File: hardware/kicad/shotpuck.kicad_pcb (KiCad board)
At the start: 2 copper layers, 37 x 37 mm, 27 parts, among them J1 Magnetic pogo 2P (female), J2 TC2030-NL, Q1 DMN63D8LDW, U1 MDBT50Q-512K, U2 LIS2DE12TR, U3 MCP73831T-2ACI/OT

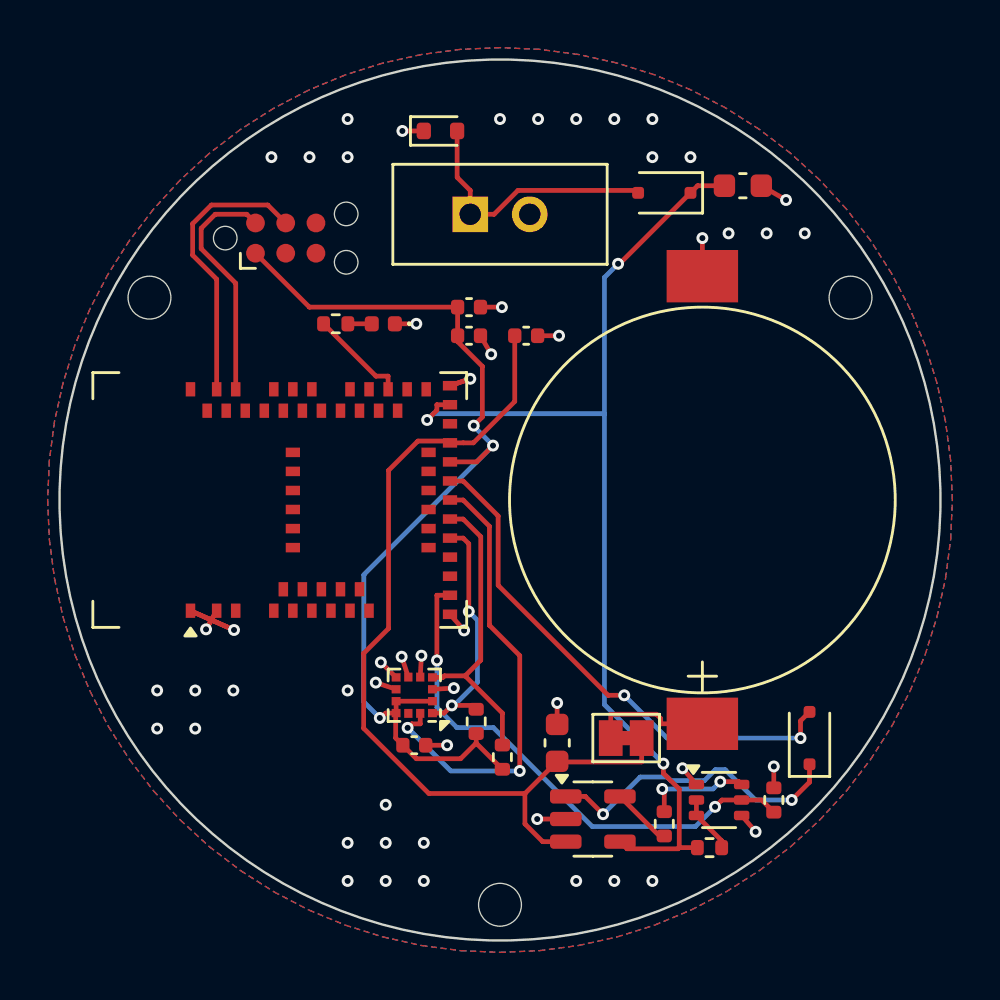
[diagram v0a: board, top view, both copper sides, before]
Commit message: Update ShotPuck to v0.2 design package
Enhancements include the integration of the LSM6DSO32 IMU, which replaces the LIS2DE12 accelerometer, allowing for 6-axis motion capture. The new CAPTURE characteristic streams raw data around each shot, improving performance metrics. The firmware and simulation have been updated to support these changes, including adjustments to the BLE protocol (v2) for better data handling. Additionally, the toolchain has been migrated to a native Windows environment for development.

Key changes:
- Updated deliverable status to v0.2.
- Added capture functionality for bow motion.
- Adjusted simulation and validation processes to reflect new hardware capabilities.
- Enhanced documentation to include new features and user requirements.

Co-Authored-By: Claude Opus 5.5 <noreply@anthropic.com>
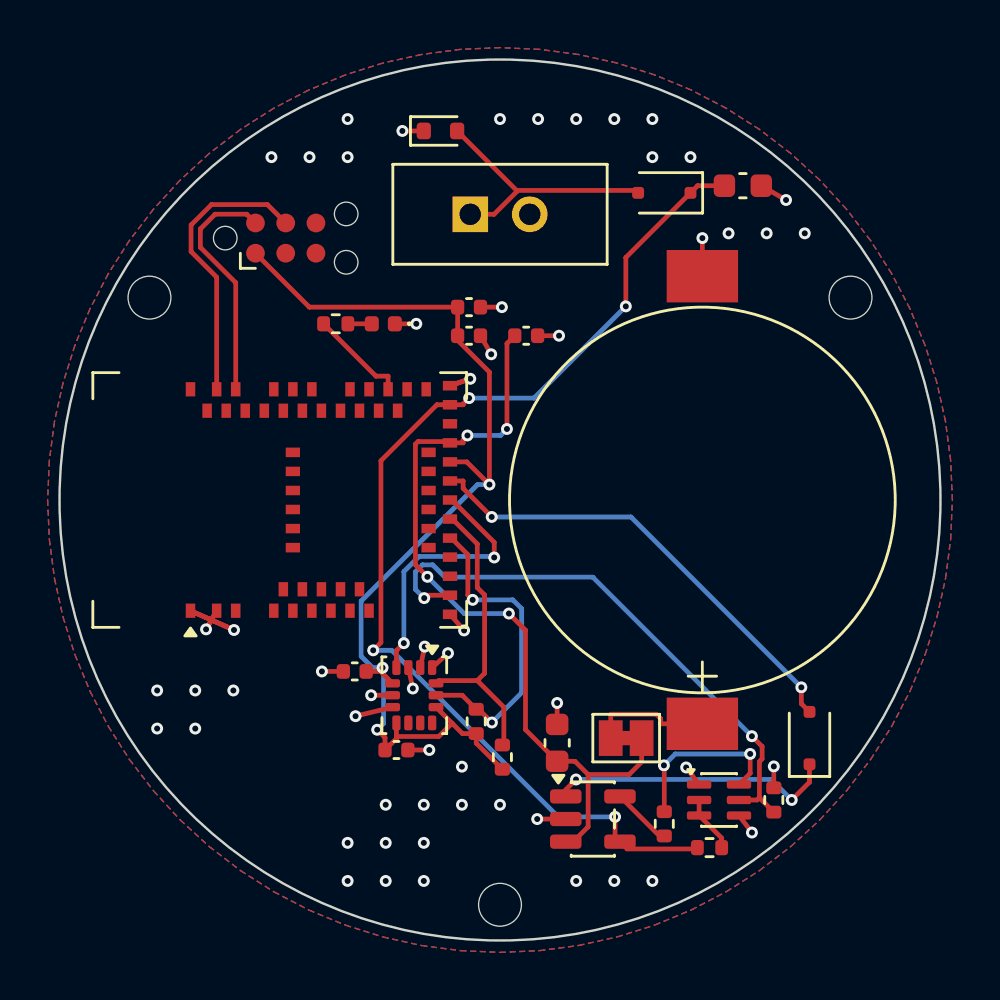
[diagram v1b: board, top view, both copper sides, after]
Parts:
- added C7: 100n, Capacitor_SMD:C_0402_1005Metric, F.Cu at (-4.35, 10.5)
- U2: value LIS2DE12TR -> LSM6DSO32TR; footprint Package_LGA:LGA-12_2x2mm_P0.5mm -> Package_LGA:LGA-14_3x2.5mm_P0.5mm_LayoutBorder3x4y
- moved C6 3.98 mm to (-6.10, 7.20), turned to 180 degrees
- turned U2 to -90 degrees
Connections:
- U2 pad 1: SCL -> GND
- U2 pad 10: VDD -> (no net)
- U2 pad 12: ACC_INT1 -> VDD
- U2 pad 2: VDD -> GND
- U2 pad 4: SDA -> ACC_INT1
- U2 pad 5: GND -> VDD
- U2 pad 8: GND -> VDD
- U2 pad 9: VDD -> (no net)
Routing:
- net ACC_INT1: track 19.4 -> 11.5 mm
- net VBAT: track 38.3 -> 33.6 mm, vias 0 -> 4
- net SCL: track 10.4 -> 13.4 mm
- net PROG_SW: track 4.50 -> 7.25 mm
- net CHG_STAT: track 22.2 -> 19.7 mm
- net CHG_INH: track 22.2 -> 24.2 mm
- net VIN: track 44.2 -> 46.1 mm, vias 3 -> 4
- net GND: track 26.0 -> 27.6 mm, vias 52 -> 56
- net VDD: track 42.0 -> 43.6 mm
- net STAT: track 13.0 -> 12.1 mm

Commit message: Add OTA, nRF52840, PCM, magnetic connector, Ø36 board and JLC panel
- Firmware: nRF52840 module (MDBT50Q-1MV2), MCUboot swap-using-move with
  ECDSA-P256 signed images, MCUmgr SMP over encrypted BLE, watchdog and
  self-confirm; 1 MB flash layout; release images shotpuck_full.hex and
  shotpuck_update.bin (v0.2.0).
- Hardware: BQ29700 + DMN2004DWK cell protection, universal CP1654 pads,
  Samzo magnetic 2-pin connector, Ø36 mm board inside the Ø40 mm puck,
  0.3 mm vias, 2x2 KiKit panel and JLCPCB BOM/CPL (gen_panel.py, gen_jlc.py).
- Mechanical: cavity sized for Varta CP1654 swell, connector chimney,
  optional brass Ø8 trim pins (balance reported with and without them).
- gen_pcb.py: stitching after all routing, connectivity rebuilt before fills,
  pre-routed Q2 drain and Q1 GND links, Freerouting optimizer off, up to 4
  board attempts until nothing is unconnected. DRC 0/0, panel DRC 0/0.

Co-Authored-By: Claude Opus 5.5 <noreply@anthropic.com>
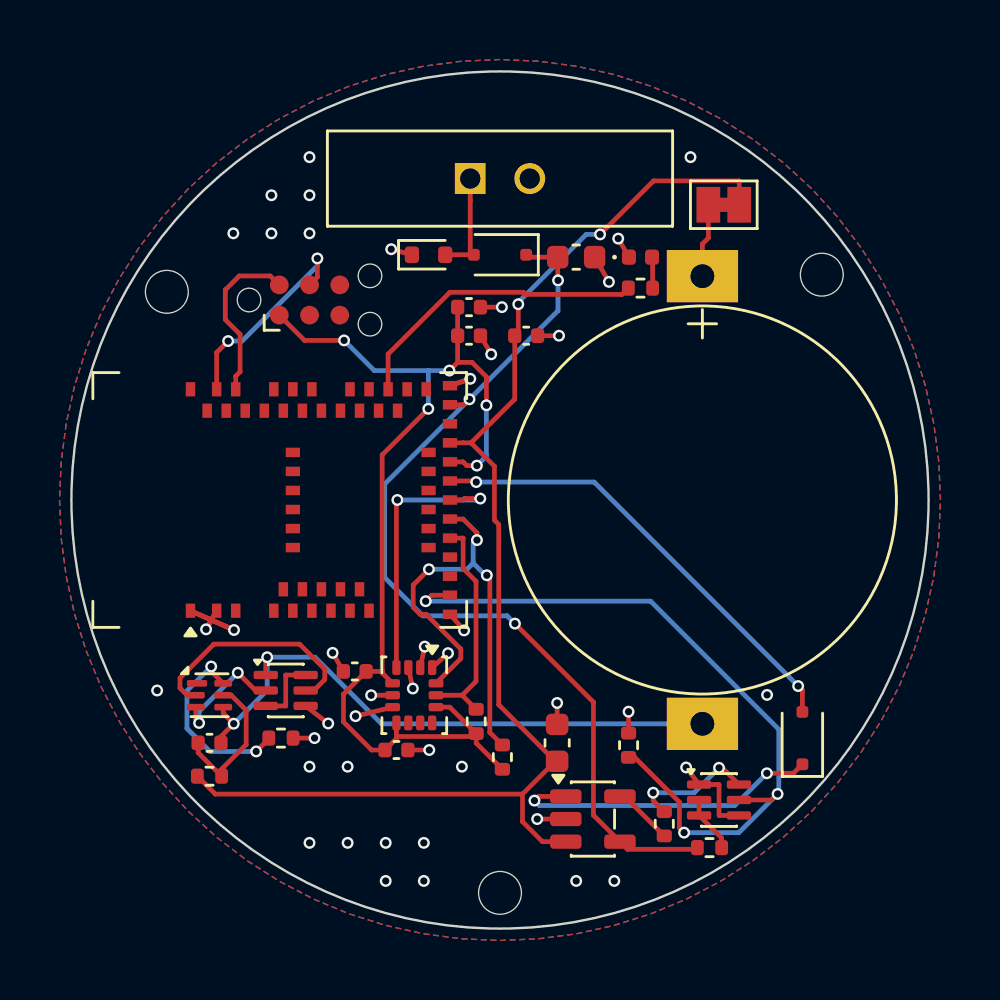
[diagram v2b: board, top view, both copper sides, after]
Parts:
- added C8: 100n, Capacitor_SMD:C_0402_1005Metric, F.Cu at (-12.2, 10.2)
- added Q2: DMN2004DWK, Package_TO_SOT_SMD:SOT-363_SC-70-6, F.Cu at (-9.00, 8.00)
- added R7: 330R, Resistor_SMD:R_0402_1005Metric, F.Cu at (-12.2, 11.6)
- added R8: 2.2k, Resistor_SMD:R_0402_1005Metric, F.Cu at (-9.20, 10.0)
- added U4: BQ29700DSER, Package_SON:WSON-6_1.5x1.5mm_P0.5mm, F.Cu at (-12.2, 8.20)
- BT1: value Varta CP1654 A3 (tabbed) -> Varta CP1654 A3 (wire or tag version); footprint ShotPuck:CP1654_Tabbed -> ShotPuck:CP1654_Pads
- J1: value Magnetic pogo 2P (female) -> Samzo PR5L4015-2P-C-F; footprint ShotPuck:MagPogo_2P -> ShotPuck:MagPogo_Samzo_2P
- U1: value MDBT50Q-512K -> MDBT50Q-1MV2
- moved JP1 22.8 mm to (9.40, -12.4)
- moved R4 12.9 mm to (5.90, -8.90)
- moved D4 11.2 mm to (5.90, -10.2), turned to 0 degrees
- moved C1 7.62 mm to (3.20, -10.2)
- moved D1 7.37 mm to (0.00, -10.3)
- moved R3 6.52 mm to (5.40, 10.3)
- moved D3 5.22 mm to (-3.00, -10.3)
- moved J2 2.79 mm to (-8.00, -8.40)
- moved H1 1.54 mm to (13.5, -9.46)
- moved J1 1.50 mm to (0.00, -13.5)
- moved H2 0.77 mm to (-14.0, -8.74)
- moved H3 0.50 mm to (0.00, 16.5)
- moved D2 0.30 mm to (12.7, 10.0)
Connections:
- BT1 pad 2: GND -> BAT_N
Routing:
- net BAT_N: track 0.00 -> 25.5 mm, vias 0 -> 2
- net VBAT: track 33.6 -> 54.2 mm, vias 4 -> 2
- net PCM_COUT: track 0.00 -> 9.75 mm
- net LED_IO: track 4.17 -> 12.8 mm
- net PCM_VM: track 0.00 -> 8.03 mm, vias 0 -> 2
- net CHG_INH: track 24.2 -> 31.5 mm, vias 2 -> 3
- net SDA: track 12.5 -> 19.3 mm, vias 0 -> 3
- net VIN: track 46.1 -> 39.4 mm, vias 4 -> 3
- net VIN_RAW: track 11.1 -> 4.40 mm
- net PCM_BAT: track 0.00 -> 6.23 mm
- net PCM_DOUT: track 0.00 -> 4.99 mm, vias 0 -> 2
- net SCL: track 13.4 -> 9.55 mm, vias 2 -> 0
- net SWDCLK: track 12.0 -> 8.84 mm, vias 0 -> 2
- net PCM_D: track 0.00 -> 2.98 mm
- net SWDIO: track 10.1 -> 7.17 mm
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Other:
- board size 37 x 37 mm -> 36 x 36 mm

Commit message: Seat the cell in a PCB notch open to the rim (puck 10.45 mm)
- The cell sits on the Kapton over the base in a notch in the PCB
  (Ø16.6 mm round end, open to the rim) instead of on top of the board,
  saving the 0.8 mm board thickness: 11.25 -> 10.45 mm, 19.8 g with the
  optional brass pins, 18.0 g without.
- Rounded relief on the + side lets the bottom (+ can) tab bend up to the
  + pad; cell pads moved to ±10.2 mm.
- Screw boss 35° -> 40° so its face stays on the board beside the notch;
  JP1 turned upright, D2 moved to the bottom centre (CHG_STAT had no route
  past the notch).
- gen_pcb.py builds the whole outline (rim arc, notch lines, arcs) and a
  copper keep-out along the notch; puck.py cuts the same shape.
- Assembly: full Kapton disc, foam/RTV between cell and cap wall.
- Board DRC 0/0, panel DRC 0/0, netlist PASS; fab, panel and JLC files
  regenerated.

Co-Authored-By: Claude Opus 5.5 <noreply@anthropic.com>
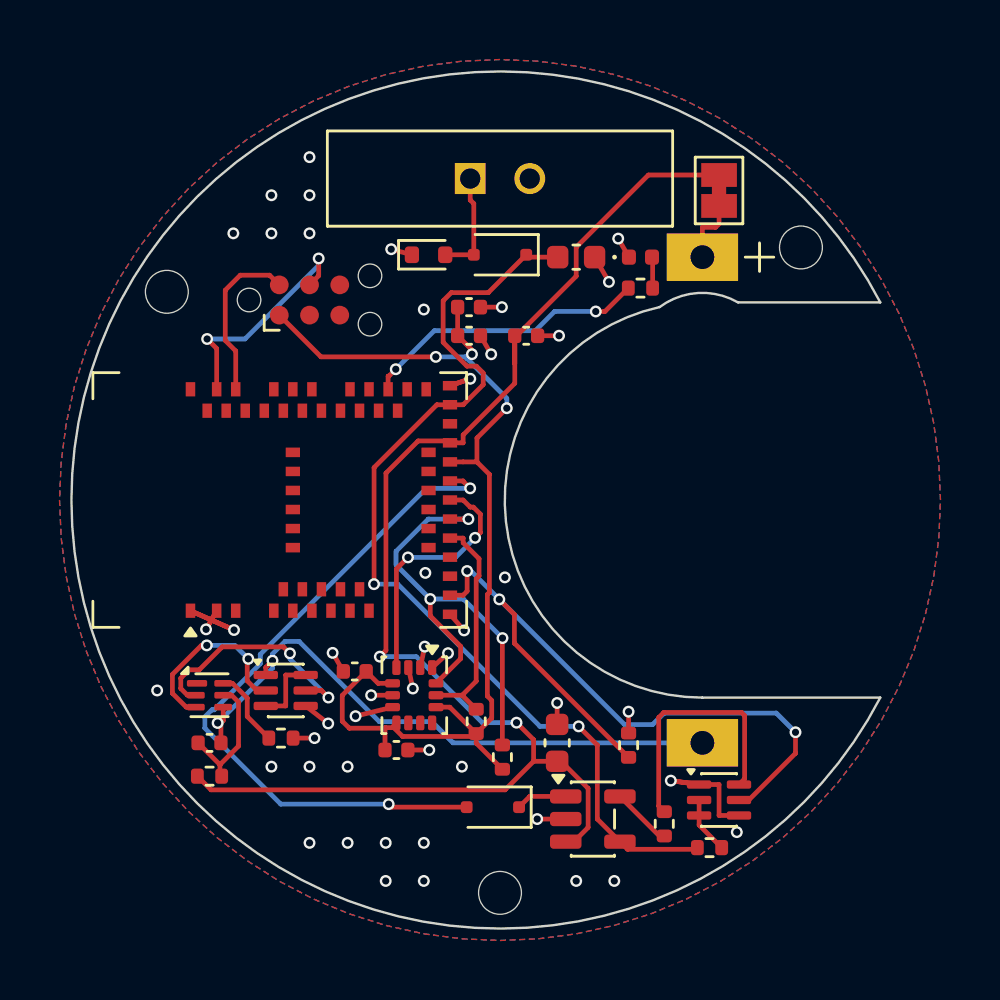
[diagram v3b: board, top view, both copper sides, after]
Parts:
- moved D2 13.3 mm to (-0.30, 12.9), turned to 180 degrees
- moved H1 1.44 mm to (12.6, -10.6)
- moved JP1 0.63 mm to (9.20, -13.0), turned to 90 degrees
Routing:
- net STAT: track 13.4 -> 2.15 mm, vias 2 -> 0
- net CHG_STAT: track 19.3 -> 29.2 mm
- net PROG_SW: track 5.32 -> 10.8 mm, vias 2 -> 0
- net VBAT: track 54.2 -> 59.5 mm
- net PCM_VM: track 8.03 -> 3.32 mm, vias 2 -> 0
- net PCM_DOUT: track 4.99 -> 7.83 mm
- net VIN: track 39.4 -> 41.1 mm, vias 3 -> 2
- net GND: track 30.2 -> 31.7 mm, vias 43 -> 46
- net ACC_INT1: track 11.9 -> 10.6 mm
- net VDD: track 45.8 -> 44.8 mm, vias 5 -> 3
- net SWDCLK: track 8.84 -> 9.80 mm
- net BAT_N: track 25.5 -> 26.3 mm
- net PCM_BAT: track 6.23 -> 5.53 mm
- net LED_IO: track 12.8 -> 12.2 mm, vias 0 -> 2
- net PCM_COUT: track 9.75 -> 10.0 mm, vias 0 -> 2
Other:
- board size 36 x 36 mm -> 34 x 36 mm

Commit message: Update ShotPuck design to rev A: replace stud with flat plate, adjust dimensions, and enhance PCB layout
- Redesigned the ShotPuck to use a 2.0 mm flat 6061 plate, bolted through a steel sleeve, improving manufacturability and cost.
- Adjusted dimensions: puck height reduced to 9.90 mm, with a center of mass 0.85 mm off-axis.
- Updated layout.json to reflect new design parameters, including cell placement and PCB notch.
- Enhanced mechanical and electrical design files, including updated battery specifications (LIR1254) and revised component placements.
- Improved documentation in HANDOVER.md and README.md to reflect changes in design and functionality.

Co-Authored-By: Claude Opus 5.5 <noreply@anthropic.com>
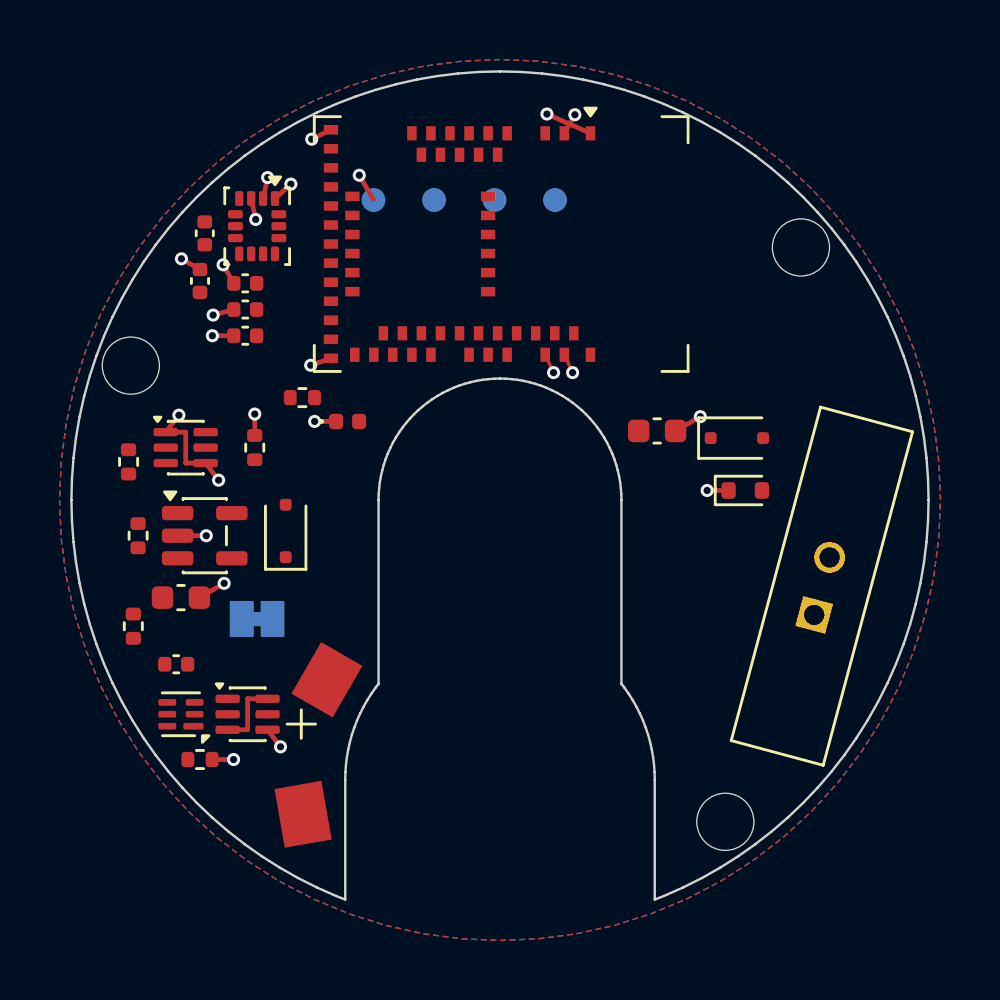
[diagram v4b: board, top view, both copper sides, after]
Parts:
- removed R5, R6: 4.7k DNP, Resistor_SMD:R_0402_1005Metric
- BT1: value Varta CP1654 A3 (wire or tag version) -> LIR1254 (plain, spring contacts); footprint ShotPuck:CP1654_Pads -> ShotPuck:LIR1254_Contacts
- H1, H2, H3: value M1.6 -> M2; footprint ShotPuck:MountingHole_1.8mm_NPTH -> ShotPuck:MountingHole_2.4mm_NPTH
- J2: value TC2030-NL -> SWD pads; footprint Connector:Tag-Connect_TC2030-IDC-NL_2x03_P1.27mm_Vertical -> ShotPuck:SWD_Pads_1x4_P2.54; moved to B.Cu
- JP1: moved to B.Cu
- R1: value 20k 1% -> 47k 1%
- moved R2 29.3 mm to (-15.6, -1.60), turned to 90 degrees
- moved Q1 26.8 mm to (-13.2, -2.20)
- moved JP1 26.5 mm to (-10.2, 5.00), turned to 180 degrees
- moved R1 25.2 mm to (-15.2, 1.50)
- moved J1 21.8 mm to (13.5, 3.62), turned to 75 degrees
- moved C7 21.4 mm to (-12.6, -9.20), turned to 90 degrees
- moved U2 20.8 mm to (-10.2, -11.5)
- moved U3 20.2 mm to (-12.4, 1.50)
- moved R3 20.1 mm to (-10.3, -2.20)
- moved C6 19.4 mm to (-12.4, -11.2), turned to 90 degrees
- moved C2 16.9 mm to (-13.4, 4.10), turned to 0 degrees
- moved D3 16.6 mm to (10.3, -0.40)
- moved R4 14.9 mm to (-8.30, -4.30)
- moved BT1 14.5 mm to (0.00, 11.8)
- moved D2 14.5 mm to (-9.00, 1.30), turned to 90 degrees
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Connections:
- J2 pad 3: (no net) -> SWDCLK
- J2 pad 4: SWDCLK -> GND
- U1 pad 20: SCL -> SDA
- U1 pad 22: SDA -> SCL
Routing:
- net VBAT: track 59.5 -> 0.00 mm, vias 2 -> 0
- net VDD: track 44.8 -> 0.00 mm, vias 3 -> 0
- net VIN: track 41.1 -> 0.00 mm, vias 2 -> 0
- net CHG_INH: track 31.6 -> 0.00 mm, vias 3 -> 0
- net CHG_STAT: track 29.2 -> 0.00 mm, vias 2 -> 0
- net BAT_N: track 26.3 -> 0.00 mm, vias 2 -> 0
- net SDA: track 19.7 -> 0.00 mm, vias 3 -> 0
- net LED_IO: track 12.2 -> 0.00 mm, vias 2 -> 0
- net PROG_SW: track 10.8 -> 0.00 mm
- net ACC_INT1: track 10.6 -> 0.00 mm, vias 2 -> 0
- net PCM_COUT: track 10.0 -> 0.00 mm, vias 2 -> 0
- net SCL: track 9.66 -> 0.00 mm
- net SWDCLK: track 9.80 -> 0.83 mm, vias 2 -> 1
- net PCM_DOUT: track 7.83 -> 0.00 mm, vias 2 -> 0
- net GND: track 31.7 -> 25.1 mm, vias 46 -> 22
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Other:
- board size 34 x 36 mm -> 36 x 34.8 mm

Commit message: Refine ShotPuck design and PCB layout for improved manufacturability
- Adjusted bolt tube hole diameter to Ø10.4 mm for JLCPCB tolerance.
- Updated PCB layout to enhance ground strategy, ensuring GND SMD pads have stubs and vias before routing.
- Revised antenna zone dimensions and keep-out areas to optimize routing space.
- Enhanced documentation in HANDOVER.md and README.md to reflect design changes and assembly instructions.
- Fixed minor discrepancies in layout.json and board_shape.py for consistency across design files.

Co-Authored-By: Claude Opus 5.5 <noreply@anthropic.com>
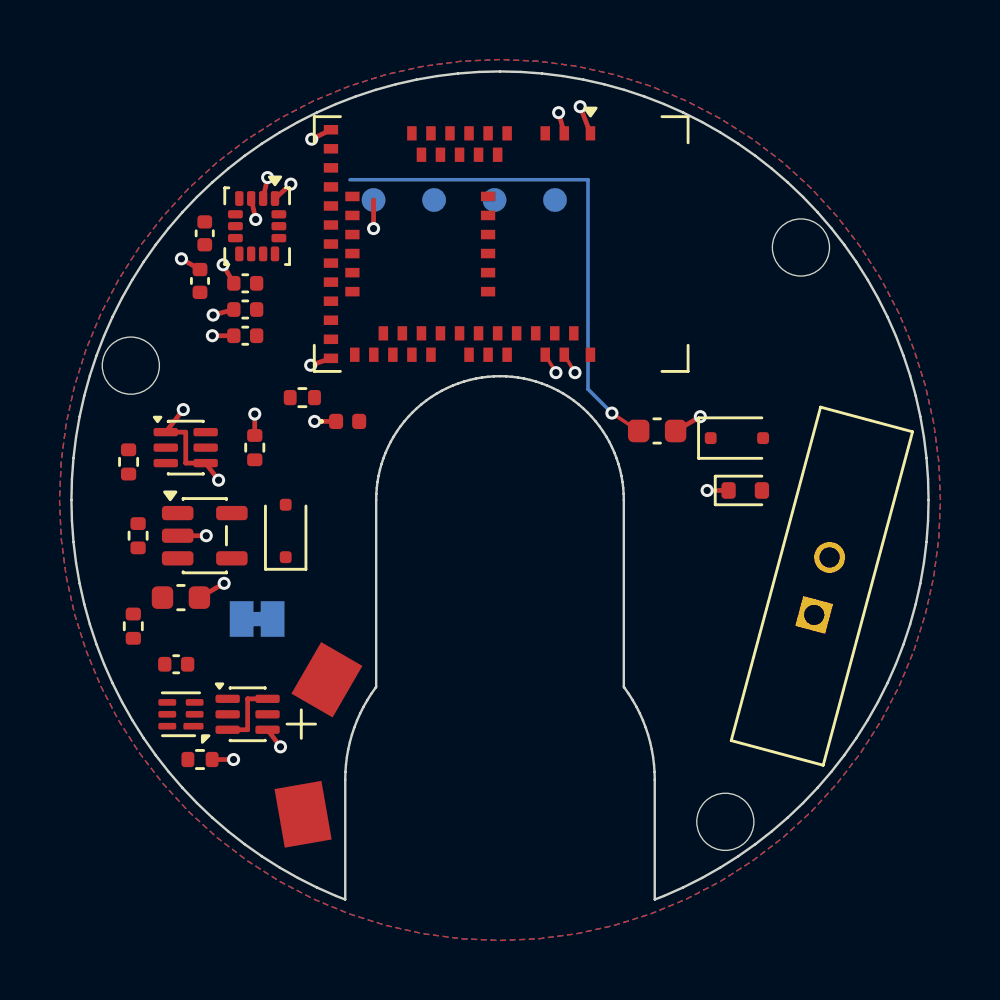
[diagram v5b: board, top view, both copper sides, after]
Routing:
- net VIN: track 0.00 -> 21.6 mm, vias 0 -> 1
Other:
- outline, holes or cut-outs redrawn
